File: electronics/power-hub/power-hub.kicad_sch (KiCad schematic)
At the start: 0 parts

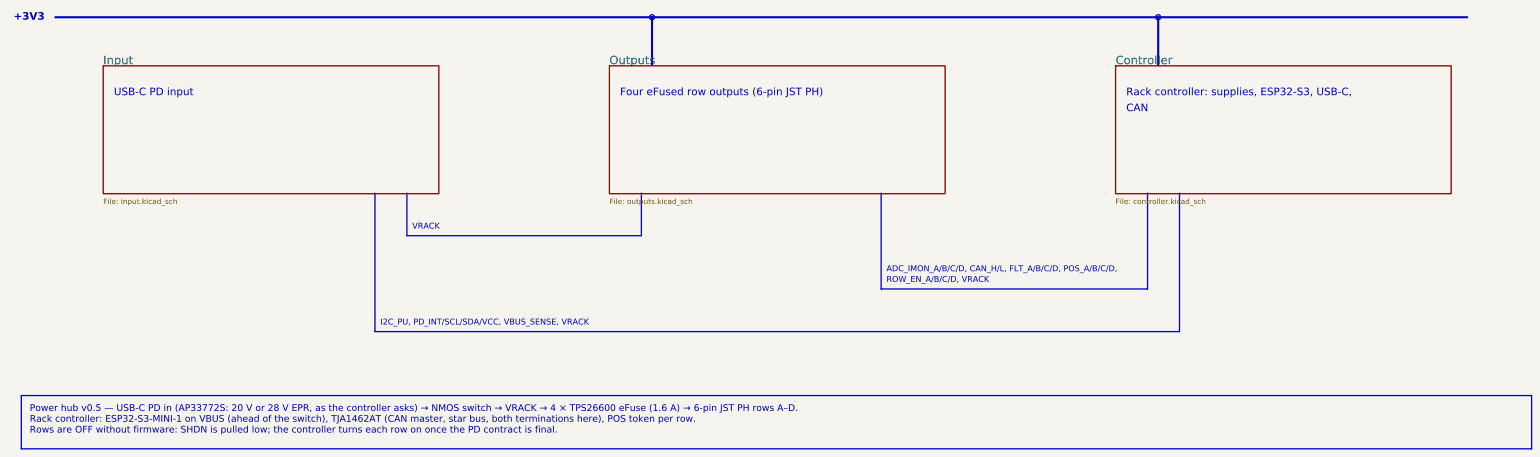
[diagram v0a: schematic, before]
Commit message: Power hub: CH224A PD sink instead of the AP33772S, no input switch
The AP33772S has no LCSC stock (Global Sourcing only).  The WCH CH224A
(C42459160, in stock) takes its place in the one-resistor mode: CFG1 6.8k
asks for 9 V at plug-in and turns I2C on, so the controller asks for 28 V
EPR (else 20 V) over I2C.  PG (open drain) keeps the PD_INT net: IO39 and
the front PD LED.  Its supply (VHV and VBUS tied) runs through 56 ohm +
1 uF: the pins are rated 32 V.

No input switch: VBUS is VRACK, and the eFuses (off until enabled, UV 15 V,
reverse blocking) do the switching.  Out: the IRF7842 pair, the 5 mohm
shunt, the NTC and their passives.  Re-routed: ERC 0, DRC 0, parity 0.
37 -> 33 part types; the hub order about $185 (BOM adjustments).  Docs:
power.md, electronics.md, sourcing.md.

Co-Authored-By: Claude Opus 5.5 <noreply@anthropic.com>
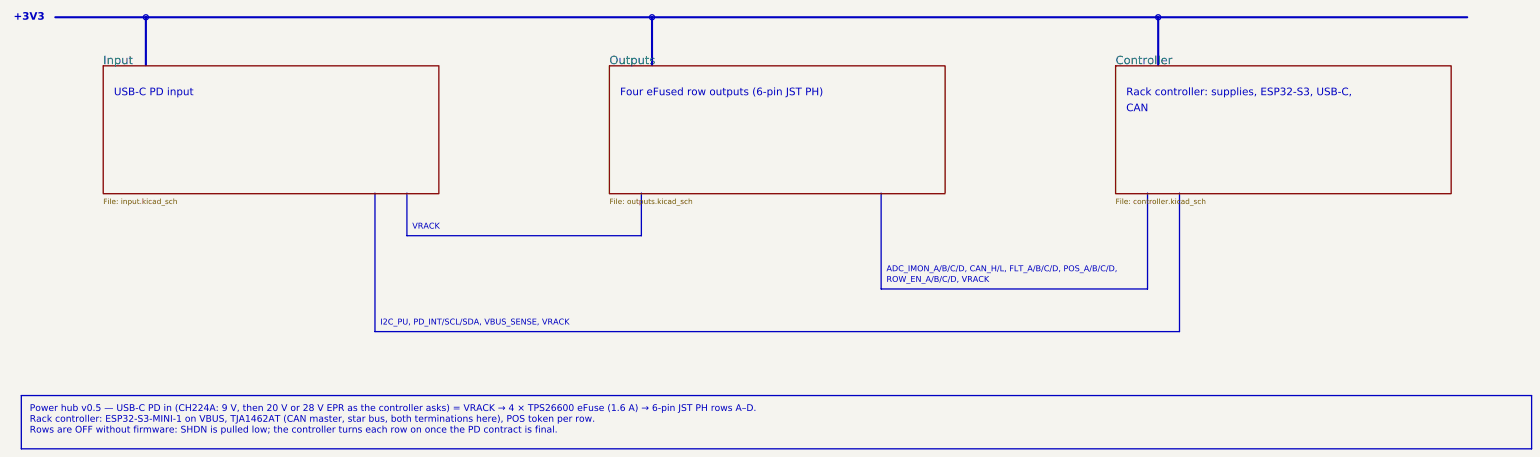
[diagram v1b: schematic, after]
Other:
- note added: "I2C_PU, PD_INT/SCL/SDA, VBUS_SENSE, VRACK"
- note removed: "I2C_PU, PD_INT/SCL/SDA/VCC, VBUS_SENSE, VRACK"
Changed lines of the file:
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@@
+	(polyline
+		(pts
+			(xy 59.69 58.42)
+			(xy 59.69 69.85)
+		)
+		(stroke
+			(width 0.5)
+			(type default)
+		)
+		(fill
+			(type none)
+		)
+	)
+	(circle
+		(center 59.69 58.42)
+		(radius 0.6)
+		(stroke
+			(width 0.3)
+			(type default)
+		)
+		(fill
+			(type outline)
+		)
+	)
 	(polyline
 		(pts
@@
 		)
 	)
-	(text "I2C_PU, PD_INT/SCL/SDA/VCC, VBUS_SENSE, VRACK"
+	(text "I2C_PU, PD_INT/SCL/SDA, VBUS_SENSE, VRACK"
 		(exclude_from_sim no)
 		(at 115.57 132.08 0)
@@
 		)
 	)
-	(text_box "Power hub v0.5 — USB-C PD in (AP33772S: 20 V or 28 V EPR, as the controller asks) → NMOS switch → VRACK → 4 × TPS26600 eFuse (1.6 A) → 6-pin JST PH rows A–D.\nRack controller: ESP32-S3-MINI-1 on VBUS (ahead of the switch), TJA1462AT (CAN master, star bus, both terminations here), POS token per row.\nRows are OFF without firmware: SHDN is pulled low; the controller turns each row on once the PD contract is final."
+	(text_box "Power hub v0.5 — USB-C PD in (CH224A: 9 V, then 20 V or 28 V EPR as the controller asks) = VRACK → 4 × TPS26600 eFuse (1.6 A) → 6-pin JST PH rows A–D.\nRack controller: ESP32-S3-MINI-1 on VBUS, TJA1462AT (CAN master, star bus, both terminations here), POS token per row.\nRows are OFF without firmware: SHDN is pulled low; the controller turns each row on once the PD contract is final."
 		(exclude_from_sim no)
 		(at 30 148.59 0)
